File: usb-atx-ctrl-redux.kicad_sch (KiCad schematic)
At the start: 16 parts, among them J1 Amphenol 54602-908LF, SW1 SX A08, SW2 SX A08, U1 AQW210EHA, U2 AQW210EHA

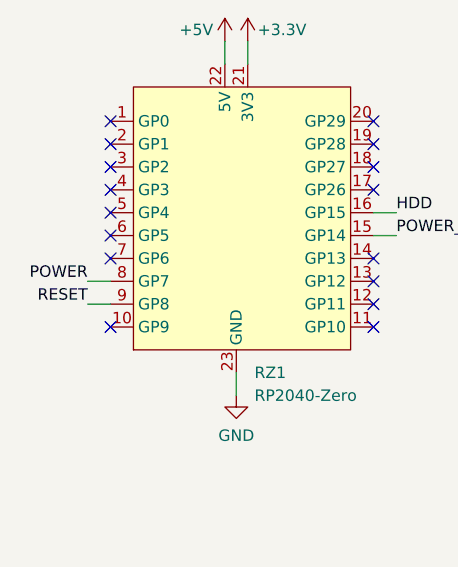
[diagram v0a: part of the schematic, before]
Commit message: Fix GPIO assignment, 8P8C footprint, bump to KiCad 8
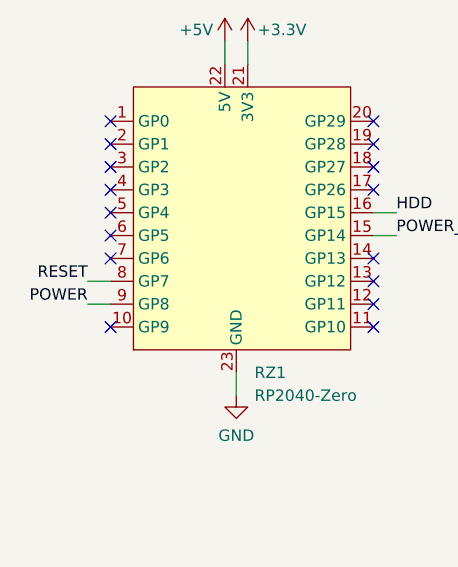
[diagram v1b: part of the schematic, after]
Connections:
- net POWER: now also RZ1.9 (GP8); no longer RZ1.8 (GP7)
- net RESET: now also RZ1.8 (GP7); no longer RZ1.9 (GP8)
